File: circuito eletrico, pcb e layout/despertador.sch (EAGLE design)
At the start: 9 parts, among them IC1 MEGA8-P

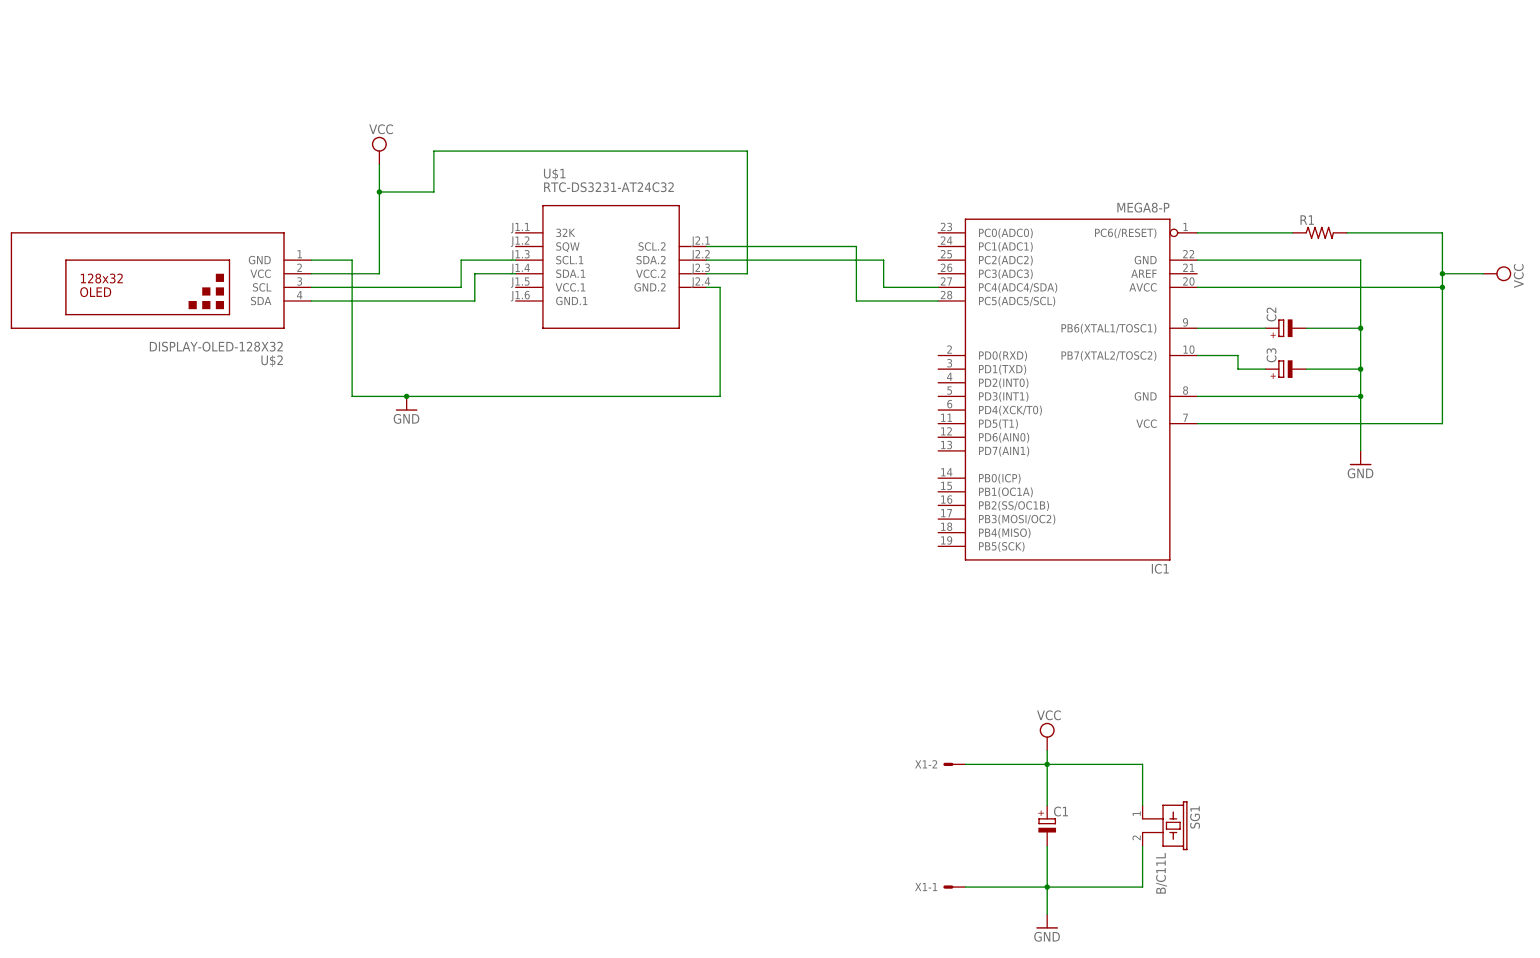
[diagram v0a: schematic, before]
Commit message: Adicionado USB nos componentes
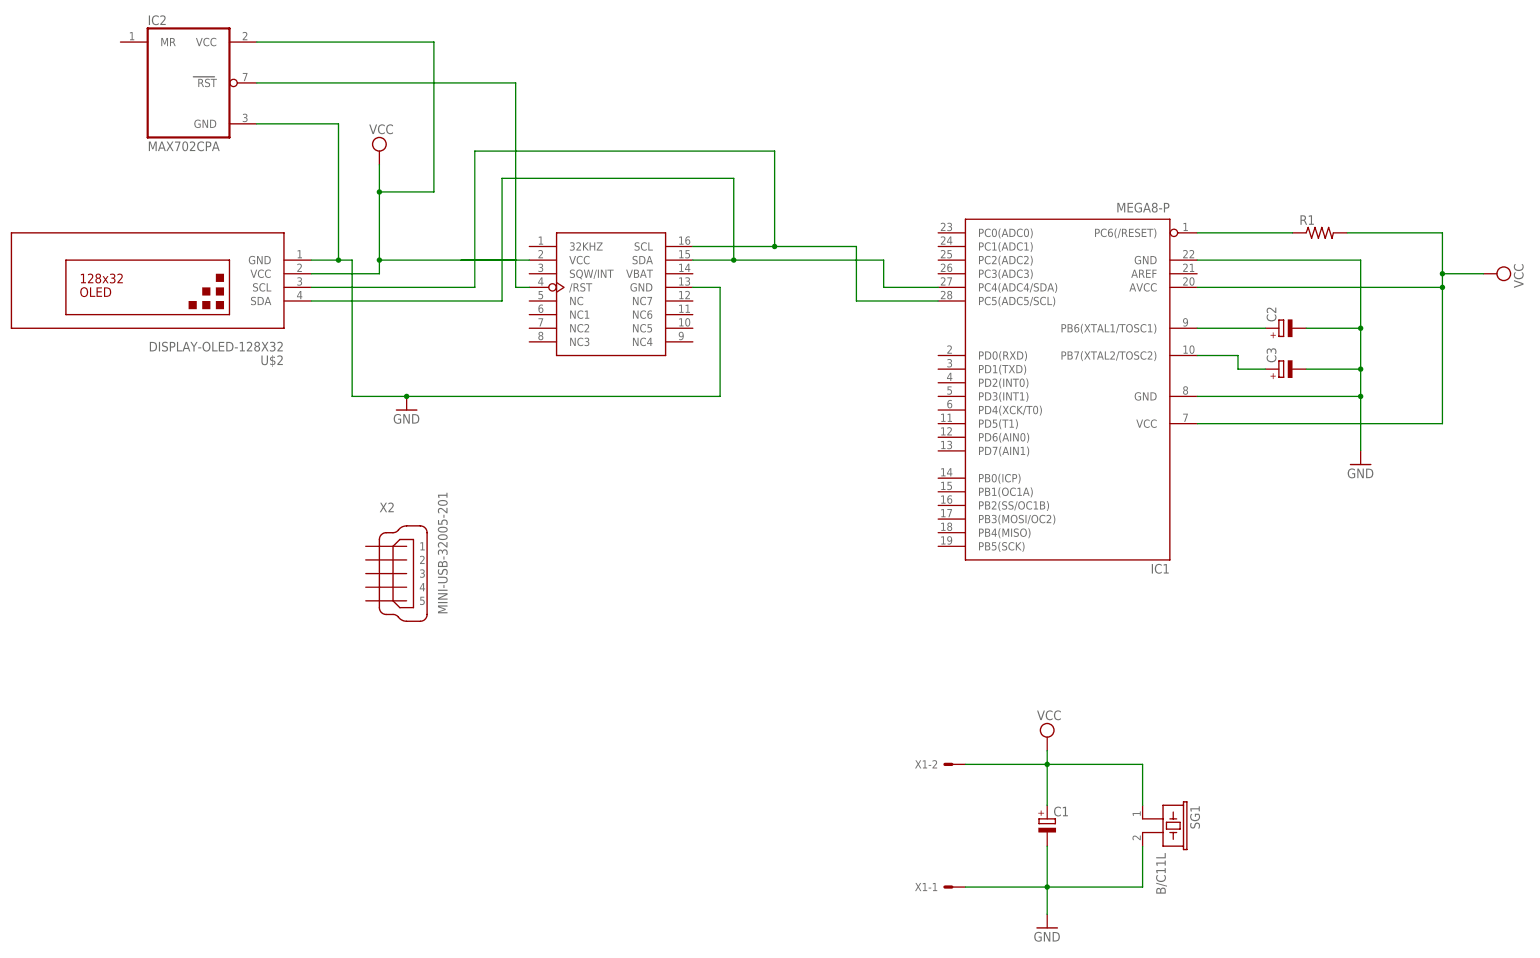
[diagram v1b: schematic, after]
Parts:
- removed U$1: RTC-DS3231-AT24C32, diy-modules:RTC-DS3231-AT24C32
- added IC2: MAX702CPA, maxim:MAX702CPA
- added U$3: DS3231, Microcontroladores:DS3231
- added X2: MINI-USB-32005-201, con-cypressindustries:MINI-USB-32005-201
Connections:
- removed net N$7: U$1.SCL.1, U$2.SCL
- net GND: now also IC2.GND, U$3.GND; no longer U$1.GND.2
- net N$1: now also U$2.SDA, U$3.SDA; no longer U$1.SDA.2
- net N$5: now also U$2.SCL, U$3.SCL; no longer U$1.SCL.2
- net N$6: now also IC2.RST, U$3./RST; no longer U$1.SDA.1, U$2.SDA
- net VCC: now also IC2.VCC, U$3.VCC; no longer U$1.VCC.2
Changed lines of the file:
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@@
 <part name="SUPPLY2" library="supply2" library_urn="urn:adsk.eagle:library:372" deviceset="VCC" device=""/>
 <part name="R1" library="rcl" library_urn="urn:adsk.eagle:library:334" deviceset="R-US_" device="0207/10" package3d_urn="urn:adsk.eagle:package:23491/2"/>
-<part name="U$1" library="diy-modules" deviceset="RTC-DS3231-AT24C32" device=""/>
 <part name="U$2" library="diy-modules" deviceset="DISPLAY-OLED-128X32" device=""/>
 <part name="GND3" library="supply1" library_urn="urn:adsk.eagle:library:371" deviceset="GND" device=""/>
 <part name="SUPPLY3" library="supply2" library_urn="urn:adsk.eagle:library:372" deviceset="VCC" device=""/>
+<part name="U$3" library="Microcontroladores" library_urn="urn:adsk.eagle:library:31052663" deviceset="DS3231" device="" package3d_urn="urn:adsk.eagle:package:31052666/2"/>
+<part name="X2" library="con-cypressindustries" library_urn="urn:adsk.eagle:library:138" deviceset="MINI-USB-" device="32005-201" package3d_urn="urn:adsk.eagle:package:6443/1"/>
+<part name="IC2" library="maxim" library_urn="urn:adsk.eagle:library:269" deviceset="MAX702CPA" device="" package3d_urn="urn:adsk.eagle:package:29519/2"/>
 </parts>
 <sheets>
@@
 <attribute name="VALUE" x="125.73" y="70.358" size="1.778" layer="96"/>
 </instance>
-<instance part="U$1" gate="G$1" x="-2.54" y="68.58" smashed="yes">
-<attribute name="NAME" x="-15.24" y="83.82" size="1.778" layer="95"/>
-<attribute name="VALUE" x="-15.24" y="81.28" size="1.778" layer="96"/>
-</instance>
 <instance part="U$2" gate="G$1" x="-88.9" y="63.5" smashed="yes" rot="R180">
 <attribute name="NAME" x="-63.5" y="50.8" size="1.778" layer="95" rot="R180"/>
@@
 <instance part="SUPPLY3" gate="G$1" x="-45.72" y="88.9" smashed="yes">
 <attribute name="VALUE" x="-47.625" y="92.075" size="1.778" layer="96"/>
+</instance>
+<instance part="U$3" gate="G$1" x="-2.54" y="58.42" smashed="yes"/>
+<instance part="X2" gate="G$1" x="-43.18" y="10.16" smashed="yes">
+<attribute name="NAME" x="-45.72" y="21.59" size="1.778" layer="95"/>
+<attribute name="VALUE" x="-33.02" y="2.54" size="1.778" layer="96" rot="R90"/>
+</instance>
+<instance part="IC2" gate="G$1" x="-81.28" y="101.6" smashed="yes">
+<attribute name="NAME" x="-88.9" y="112.395" size="1.778" layer="95"/>
+<attribute name="VALUE" x="-88.9" y="88.9" size="1.778" layer="96"/>
 </instance>
 </instances>
@@
 <segment>
 <pinref part="U$2" gate="G$1" pin="GND"/>
-<wire x1="-58.42" y1="68.58" x2="-50.8" y2="68.58" width="0.1524" layer="91"/>
+<wire x1="-58.42" y1="68.58" x2="-53.34" y2="68.58" width="0.1524" layer="91"/>
+<wire x1="-53.34" y1="68.58" x2="-50.8" y2="68.58" width="0.1524" layer="91"/>
 <wire x1="-50.8" y1="68.58" x2="-50.8" y2="43.18" width="0.1524" layer="91"/>
 <pinref part="GND3" gate="1" pin="GND"/>
@@
 <wire x1="-40.64" y1="43.18" x2="17.78" y2="43.18" width="0.1524" layer="91"/>
 <junction x="-40.64" y="43.18"/>
-<pinref part="U$1" gate="G$1" pin="GND.2"/>
 <wire x1="17.78" y1="43.18" x2="17.78" y2="63.5" width="0.1524" layer="91"/>
-<wire x1="17.78" y1="63.5" x2="15.24" y2="63.5" width="0.1524" layer="91"/>
+<pinref part="U$3" gate="G$1" pin="GND"/>
+<wire x1="17.78" y1="63.5" x2="12.7" y2="63.5" width="0.1524" layer="91"/>
+<pinref part="IC2" gate="G$1" pin="GND"/>
+<wire x1="-68.58" y1="93.98" x2="-53.34" y2="93.98" width="0.1524" layer="91"/>
+<wire x1="-53.34" y1="68.58" x2="-53.34" y2="93.98" width="0.1524" layer="91"/>
+<junction x="-53.34" y="68.58"/>
 </segment>
 </net>
@@
 <segment>
 <pinref part="SUPPLY3" gate="G$1" pin="VCC"/>
+<pinref part="U$2" gate="G$1" pin="VCC"/>
 <wire x1="-45.72" y1="86.36" x2="-45.72" y2="81.28" width="0.1524" layer="91"/>
-<pinref part="U$2" gate="G$1" pin="VCC"/>
-<wire x1="-45.72" y1="81.28" x2="-45.72" y2="66.04" width="0.1524" layer="91"/>
+<wire x1="-45.72" y1="81.28" x2="-45.72" y2="68.58" width="0.1524" layer="91"/>
+<wire x1="-45.72" y1="68.58" x2="-45.72" y2="66.04" width="0.1524" layer="91"/>
 <wire x1="-45.72" y1="66.04" x2="-58.42" y2="66.04" width="0.1524" layer="91"/>
-<pinref part="U$1" gate="G$1" pin="VCC.2"/>
-<wire x1="15.24" y1="66.04" x2="22.86" y2="66.04" width="0.1524" layer="91"/>
-<wire x1="22.86" y1="66.04" x2="22.86" y2="88.9" width="0.1524" layer="91"/>
-<wire x1="22.86" y1="88.9" x2="-35.56" y2="88.9" width="0.1524" layer="91"/>
-<wire x1="-35.56" y1="88.9" x2="-35.56" y2="81.28" width="0.1524" layer="91"/>
+<pinref part="U$3" gate="G$1" pin="VCC"/>
+<wire x1="-17.78" y1="68.58" x2="-45.72" y2="68.58" width="0.1524" layer="91"/>
+<junction x="-45.72" y="68.58"/>
+<pinref part="IC2" gate="G$1" pin="VCC"/>
+<wire x1="-68.58" y1="109.22" x2="-35.56" y2="109.22" width="0.1524" layer="91"/>
+<wire x1="-35.56" y1="109.22" x2="-35.56" y2="81.28" width="0.1524" layer="91"/>
 <wire x1="-35.56" y1="81.28" x2="-45.72" y2="81.28" width="0.1524" layer="91"/>
 <junction x="-45.72" y="81.28"/>
@@
 <net name="N$1" class="0">
 <segment>
-<pinref part="U$1" gate="G$1" pin="SDA.2"/>
-<wire x1="15.24" y1="68.58" x2="48.26" y2="68.58" width="0.1524" layer="91"/>
+<wire x1="12.7" y1="68.58" x2="20.32" y2="68.58" width="0.1524" layer="91"/>
+<wire x1="20.32" y1="68.58" x2="48.26" y2="68.58" width="0.1524" layer="91"/>
 <wire x1="48.26" y1="68.58" x2="48.26" y2="63.5" width="0.1524" layer="91"/>
 <pinref part="IC1" gate="G$1" pin="PC4(ADC4/SDA)"/>
 <wire x1="48.26" y1="63.5" x2="58.42" y2="63.5" width="0.1524" layer="91"/>
+<pinref part="U$3" gate="G$1" pin="SDA"/>
+<pinref part="U$2" gate="G$1" pin="SDA"/>
+<wire x1="-58.42" y1="60.96" x2="-22.86" y2="60.96" width="0.1524" layer="91"/>
+<wire x1="-22.86" y1="60.96" x2="-22.86" y2="83.82" width="0.1524" layer="91"/>
+<wire x1="-22.86" y1="83.82" x2="20.32" y2="83.82" width="0.1524" layer="91"/>
+<wire x1="20.32" y1="83.82" x2="20.32" y2="68.58" width="0.1524" layer="91"/>
+<junction x="20.32" y="68.58"/>
 </segment>
 </net>
 <net name="N$5" class="0">
 <segment>
-<pinref part="U$1" gate="G$1" pin="SCL.2"/>
-<wire x1="15.24" y1="71.12" x2="43.18" y2="71.12" width="0.1524" layer="91"/>
+<wire x1="12.7" y1="71.12" x2="27.94" y2="71.12" width="0.1524" layer="91"/>
+<wire x1="27.94" y1="71.12" x2="43.18" y2="71.12" width="0.1524" layer="91"/>
 <wire x1="43.18" y1="71.12" x2="43.18" y2="60.96" width="0.1524" layer="91"/>
 <pinref part="IC1" gate="G$1" pin="PC5(ADC5/SCL)"/>
 <wire x1="43.18" y1="60.96" x2="58.42" y2="60.96" width="0.1524" layer="91"/>
+<pinref part="U$3" gate="G$1" pin="SCL"/>
+<pinref part="U$2" gate="G$1" pin="SCL"/>
+<wire x1="-58.42" y1="63.5" x2="-27.94" y2="63.5" width="0.1524" layer="91"/>
+<wire x1="-27.94" y1="63.5" x2="-27.94" y2="88.9" width="0.1524" layer="91"/>
+<wire x1="-27.94" y1="88.9" x2="27.94" y2="88.9" width="0.1524" layer="91"/>
+<wire x1="27.94" y1="88.9" x2="27.94" y2="71.12" width="0.1524" layer="91"/>
+<junction x="27.94" y="71.12"/>
+</segment>
+</net>
+<net name="N$8" class="0">
+<segment>
+<wire x1="-30.48" y1="68.58" x2="-20.32" y2="68.58" width="0.1524" layer="91"/>
 </segment>
 </net>
 <net name="N$6" class="0">
 <segment>
-<pinref part="U$2" gate="G$1" pin="SDA"/>
-<wire x1="-58.42" y1="60.96" x2="-27.94" y2="60.96" width="0.1524" layer="91"/>
-<wire x1="-27.94" y1="60.96" x2="-27.94" y2="66.04" width="0.1524" layer="91"/>
-<pinref part="U$1" gate="G$1" pin="SDA.1"/>
-<wire x1="-27.94" y1="66.04" x2="-20.32" y2="66.04" width="0.1524" layer="91"/>
-</segment>
-</net>
-<net name="N$7" class="0">
-<segment>
-<pinref part="U$2" gate="G$1" pin="SCL"/>
-<wire x1="-58.42" y1="63.5" x2="-30.48" y2="63.5" width="0.1524" layer="91"/>
-<wire x1="-30.48" y1="63.5" x2="-30.48" y2="68.58" width="0.1524" layer="91"/>
-<pinref part="U$1" gate="G$1" pin="SCL.1"/>
-<wire x1="-30.48" y1="68.58" x2="-20.32" y2="68.58" width="0.1524" layer="91"/>
-</segment>
-</net>
+<pinref part="U$3" gate="G$1" pin="/RST"/>
+<wire x1="-17.78" y1="63.5" x2="-20.32" y2="63.5" width="0.1524" layer="91"/>
+<wire x1="-20.32" y1="63.5" x2="-20.32" y2="101.6" width="0.1524" layer="91"/>
+<pinref part="IC2" gate="G$1" pin="RST"/>
+<wire x1="-20.32" y1="101.6" x2="-68.58" y2="101.6" width="0.1524" layer="91"/>
+</segment>
+</net>
